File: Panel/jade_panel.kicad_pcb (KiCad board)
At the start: 2 copper layers, 15 x 128.5 mm, 0 parts

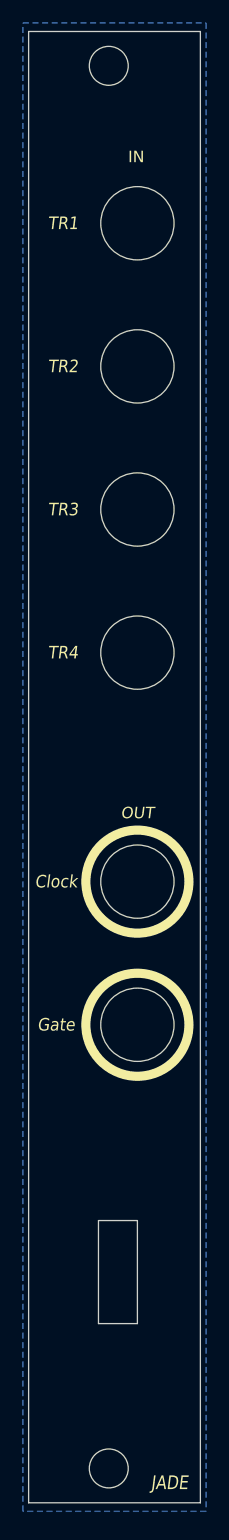
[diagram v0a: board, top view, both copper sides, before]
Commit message: PCB Panel for Rev.B
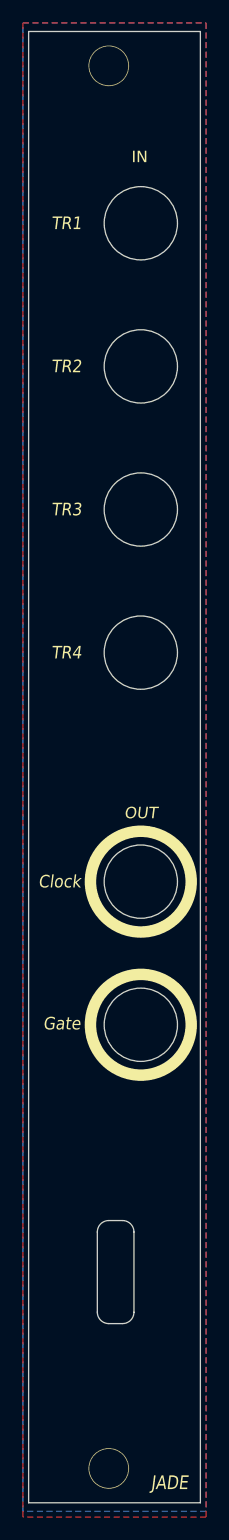
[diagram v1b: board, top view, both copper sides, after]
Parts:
- added H1: MountingHole_Pad, Akiyuki_Footprint:MountingHole_3.4mm, F.Cu at (109.5, 43.8)
- added H2: MountingHole_Pad, Akiyuki_Footprint:MountingHole_3.4mm, F.Cu at (109.5, 166.2)
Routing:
- added copper zone on B.Cu, net GND
- added copper zone on F.Cu, net GND
- removed copper zone on B.Cu, net (none)
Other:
- outline, holes or cut-outs redrawn
- board text added: "JLCJLCJLCJLC"
